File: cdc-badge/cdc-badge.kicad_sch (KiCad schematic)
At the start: 156 parts, among them J1 USB_C, J2 JST S2B-PH-SM4-TB, J3 Conn_02x20_Odd_Even, J4 Conn_Grove, J5 Conn_02x03_Odd_Even, J6 Conn_01x06, J7 Conn_01x24, Q1 Si1308EDL, Q2 Si1308EDL, SW0 0, SW1 1, SW10 YES, SW11 NO, SW12 power on/reset, SW13 reset, SW14 flash/power off, SW15 MST-22D18G2 3J, SW16 MST-22D18G2 3J, SW17 MS-22D28-G020, SW2 2, SW3 3, SW4 4, SW5 5, SW6 6, SW7 7, SW8 8, SW9 9, U1 ESP32-S3-WROOM-1-N16R8, U2 TCA9535PWR, U3 TR01-C2P-T301, U5 TLV61070ADBVR, U6 BQ25895RTW, U7 USBLC6-2SC6, U8 TLV62569DBV

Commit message: PCB. Schem: changed TP to smaller FP
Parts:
- TP1, TP10, TP2, TP3, TP8, TP9: footprint TestPoint:TestPoint_Pad_D2.0mm -> TestPoint:TestPoint_Pad_D1.5mm
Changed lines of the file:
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@@
 			)
 		)
-		(property "Footprint" "TestPoint:TestPoint_Pad_D2.0mm"
+		(property "Footprint" "TestPoint:TestPoint_Pad_D1.5mm"
 			(at 180.34 54.61 0)
 			(effects
@@
 			)
 		)
-		(property "Footprint" "TestPoint:TestPoint_Pad_D2.0mm"
+		(property "Footprint" "TestPoint:TestPoint_Pad_D1.5mm"
 			(at 73.66 82.55 0)
 			(effects
@@
 			)
 		)
-		(property "Footprint" "TestPoint:TestPoint_Pad_D2.0mm"
+		(property "Footprint" "TestPoint:TestPoint_Pad_D1.5mm"
 			(at 54.61 44.45 0)
 			(effects
@@
 			)
 		)
-		(property "Footprint" "TestPoint:TestPoint_Pad_D2.0mm"
+		(property "Footprint" "TestPoint:TestPoint_Pad_D1.5mm"
 			(at 166.37 71.12 0)
 			(effects
@@
 			)
 		)
-		(property "Footprint" "TestPoint:TestPoint_Pad_D2.0mm"
+		(property "Footprint" "TestPoint:TestPoint_Pad_D1.5mm"
 			(at 156.21 64.77 0)
 			(effects
@@
 			)
 		)
-		(property "Footprint" "TestPoint:TestPoint_Pad_D2.0mm"
+		(property "Footprint" "TestPoint:TestPoint_Pad_D1.5mm"
 			(at 83.82 85.09 0)
 			(effects

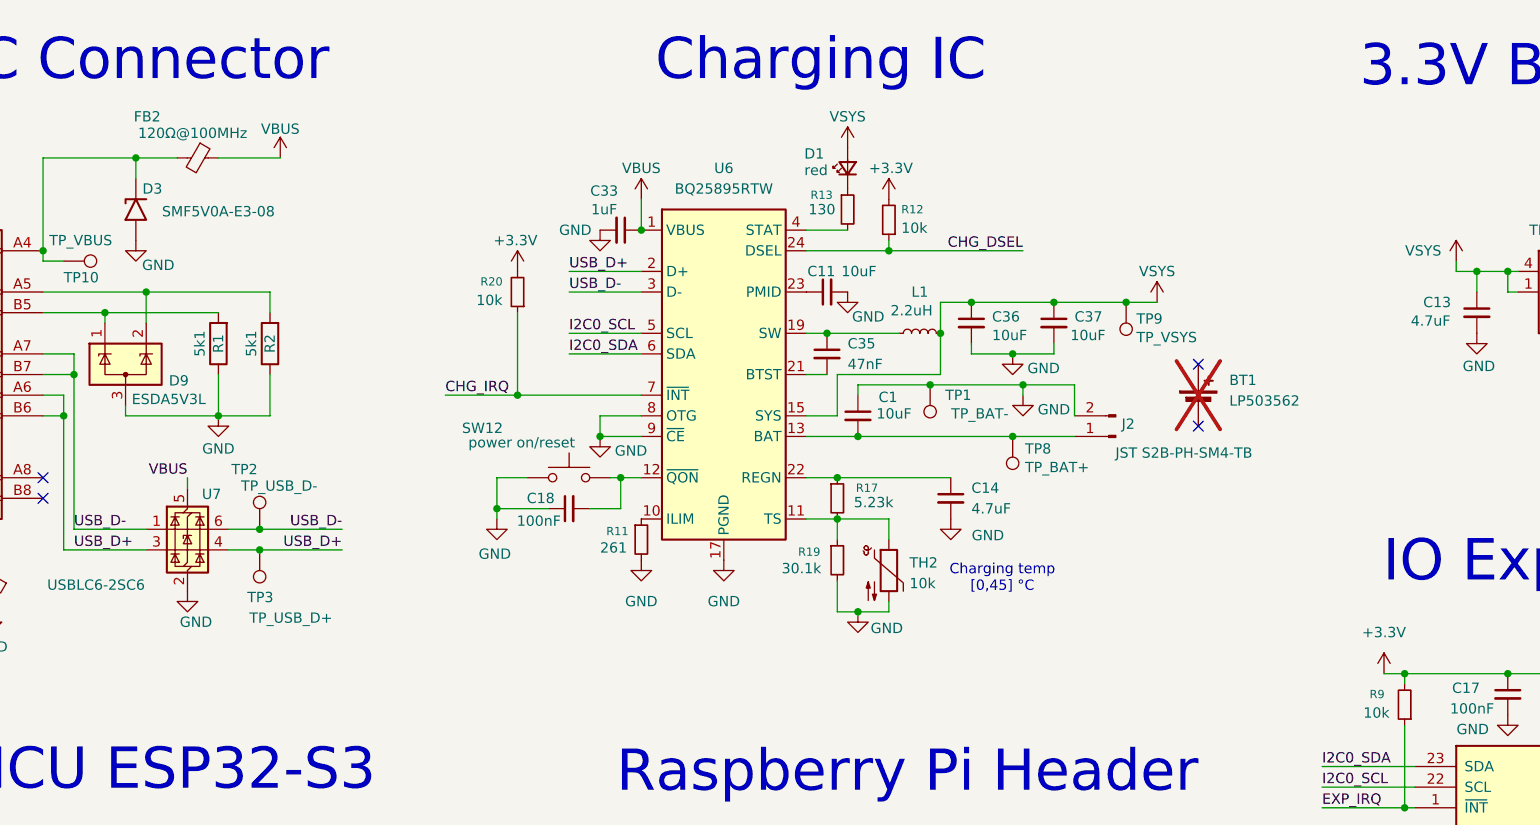
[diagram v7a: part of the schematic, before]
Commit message: schematic: ceetee reviews, charging IC
Lower status LED current and connect to stable voltage source.
Use standard values for config resistors.
Add pull-downs to OTG and CE to allow hacking.
Warn about need to set max charge current in firmware.
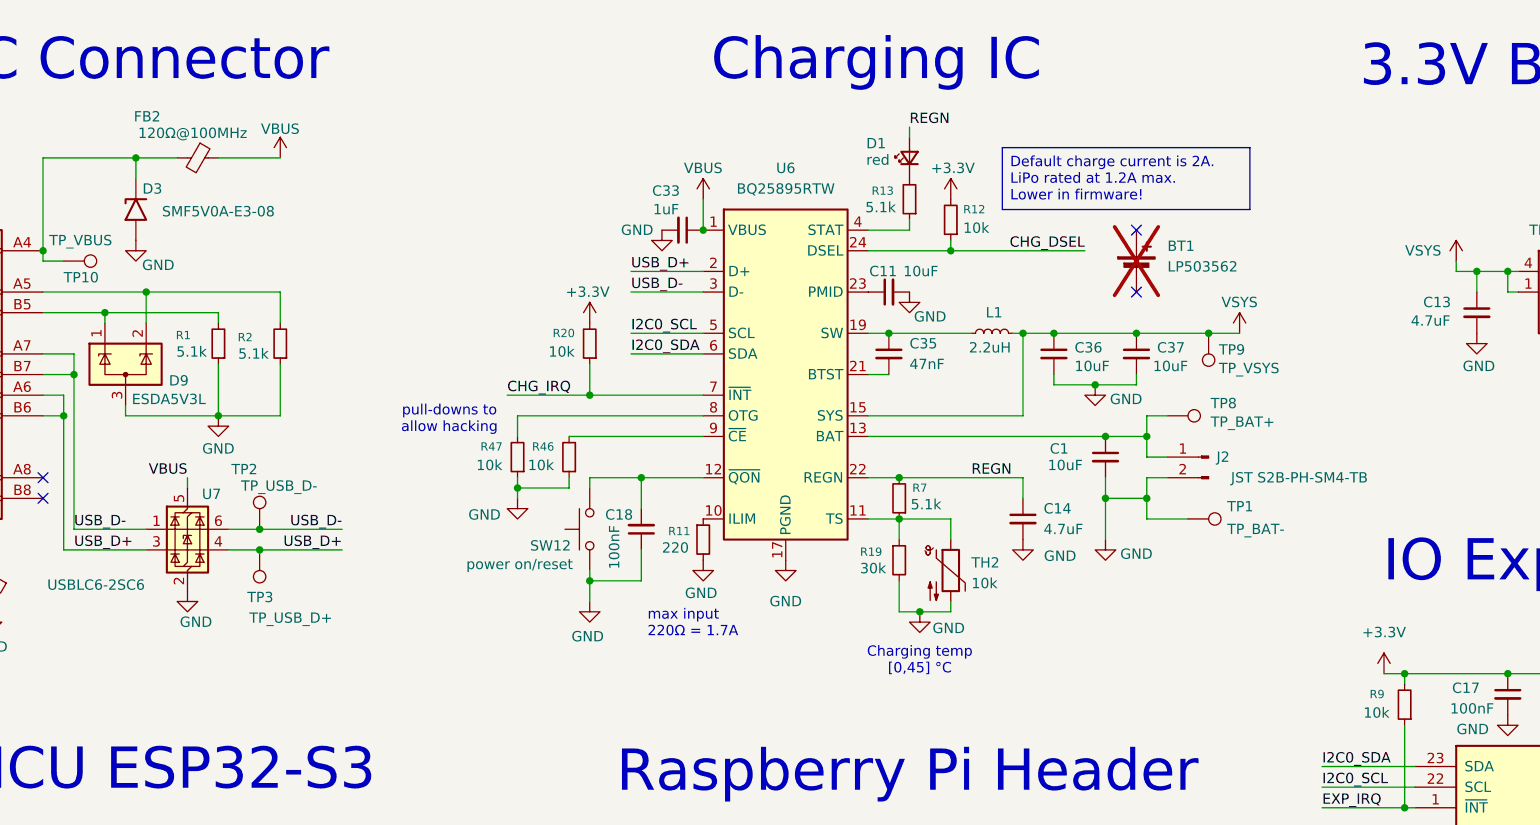
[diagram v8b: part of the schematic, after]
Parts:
- removed R17: 5.23k, Resistor_SMD:R_0603_1608Metric, symbol Device:R_Small
- removed R2: 5k1, Resistor_SMD:R_0603_1608Metric, symbol Device:R
- added R2, R7: 5.1k, Resistor_SMD:R_0603_1608Metric, symbol Device:R_Small
- added R46, R47: 10k, Resistor_SMD:R_0603_1608Metric, symbol Device:R_Small
- R1: value 5k1 -> 5.1k; symbol Device:R -> Device:R_Small; MPN (none) -> 0603WAF5101T5E
- R11: value 261 -> 220; JLCPCB PN C321816 -> C22962; MPN (none) -> 0603WAF2200T5E
- R13: value 130 -> 5.1k; JLCPCB PN C294647 -> C23186; MPN (none) -> 0603WAF5101T5E
- R19: value 30.1k -> 30k; JLCPCB PN C23000 -> C22984; MPN (none) -> 0603WAF3002T5E
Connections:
- net GND: now also C1.2, R2.1, R46.1, R47.1; no longer C1.1, U6.8 (OTG), U6.9 (~{CE})
- net VSYS: no longer D1.2 (A)
- net at D1.1 (K): now also R13.2; no longer R13.1
- net at U6.4 (STAT): now also R13.1; no longer R13.2
- net REGN: now reaches C14.1, U6.22 (REGN)
- net REGN: now also D1.2 (A), R7.2
- net at R19.1, TH2.1, U6.11 (TS): now also R7.1
- net at D9.2 (K), J1.A5 (CC1): now also R2.2
- net at J2.1 (Pin_1), TP8.1, U6.13 (BAT)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: now also C1.1; no longer C1.2
- new net: R46.2, U6.9 (~{CE})
- new net: R47.2, U6.8 (OTG)
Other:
- note added: "max input 220Ω = 1.7A"
- note added: "pull-downs to allow hacking"
- moved on the sheet: BT1, C1, C11, C14, C18, C33, C35, C36, C37, D1, J2, L1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
